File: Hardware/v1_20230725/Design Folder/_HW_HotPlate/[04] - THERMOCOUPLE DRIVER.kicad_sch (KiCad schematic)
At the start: 10 parts, among them J401 RCPT_2POS_2.54MM_VERT, U401 MAX31855JASA+T

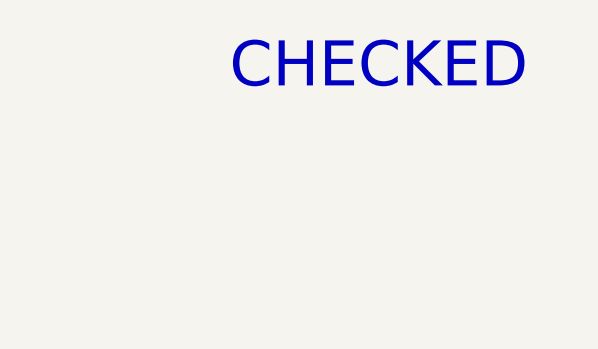
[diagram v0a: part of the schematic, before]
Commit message: Schematic library has been updated
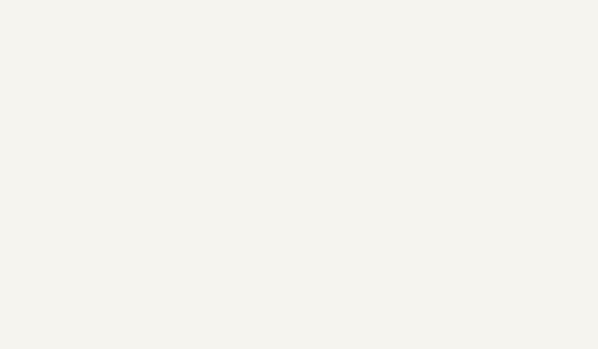
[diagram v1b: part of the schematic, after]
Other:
- note removed: "CHECKED"
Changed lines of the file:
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@@
 (kicad_sch (version 20230121) (generator eeschema)
-  (paper "B")
+  (paper "C")
   (title_block
     (title "Hot Plate")
@@
     (company "Mend0z0")
     (comment 1 "v1")
+    (comment 2 "RELEASED")
     (comment 3 "Siavash Taher Parvar")
     (comment 8 "N/A")
@@
     (effects (font (size 1.27 1.27)) (justify left bottom))
   )
-  (text "CHECKED" (at 378.46 38.1 0)
-    (effects (font (size 5 5)) (justify left bottom))
-  )
   (text "DESIGN NOTE:\n\nIt is strongly recommended \nto add a 10nF ceramic surface-mount\ndifferential capacitor, placed across\nthe T+ and T- pins, in order to \nfilter noise on the thermocouple lines.\n"

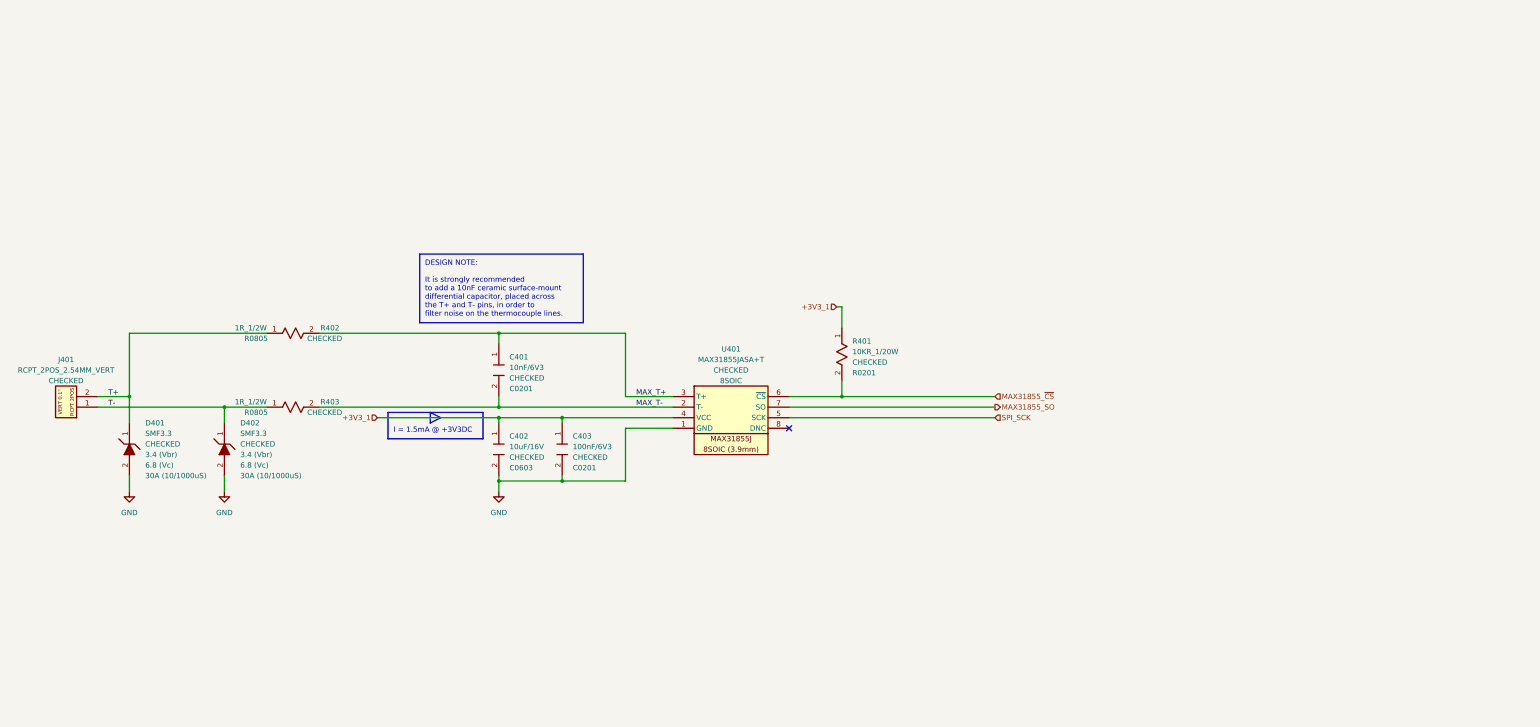
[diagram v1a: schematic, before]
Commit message: components have been updated
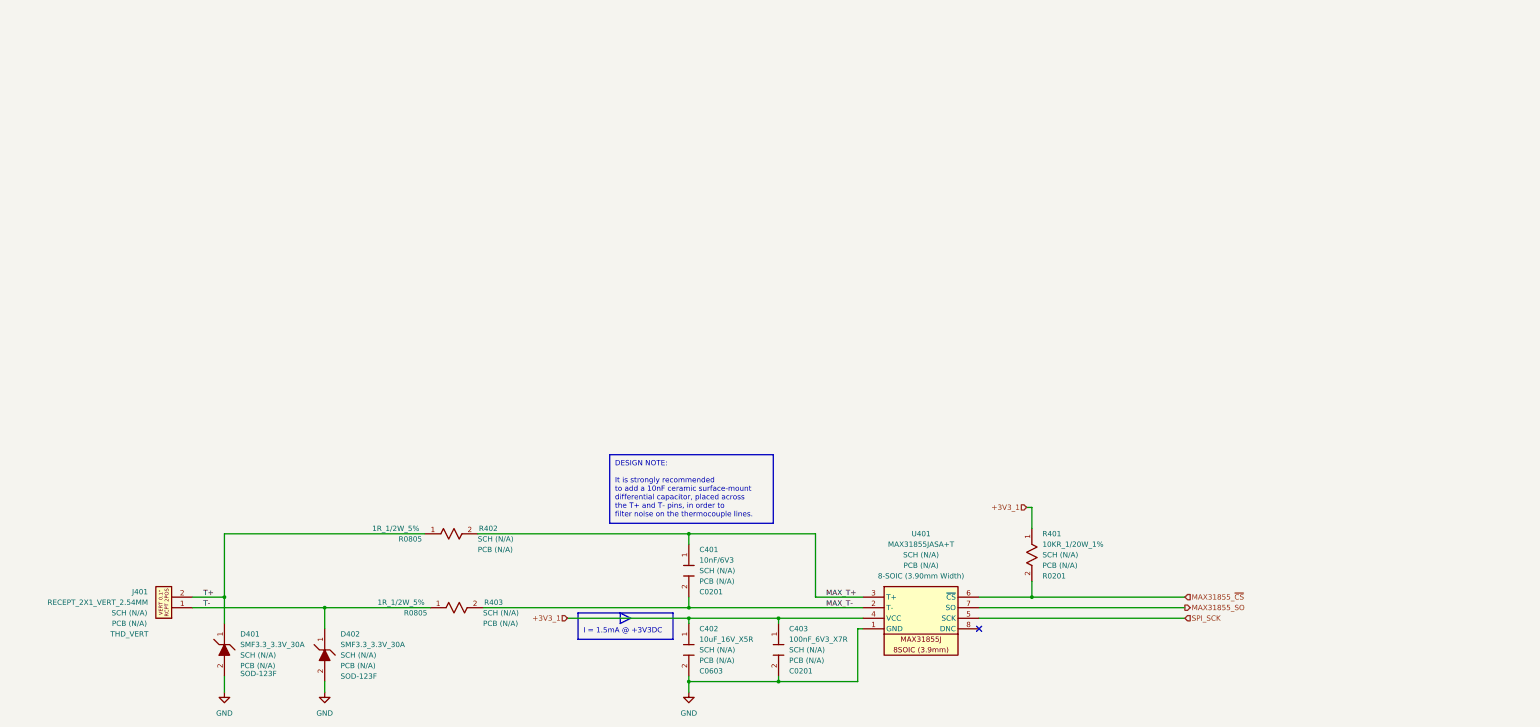
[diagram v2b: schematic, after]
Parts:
- C401: symbol _SCHLIB_HotPlate:CAP_10nF/6V3-C0201 -> _SCHLIB_HotPlate:CAP_10nF_6V3_X7R_C0201; Manufacturer (none) -> Walsin Technology Corporation; PCB CHECk (none) -> PCB (N/A); Part Number 0201B103K6R3CT -> (none); Part Number (Manufacturer) (none) -> 0201B103K6R3CT; Part Number (Vendor) (none) -> 1292-1120-2-ND; SCH CHECK CHECKED -> SCH (N/A); Vendor (none) -> Digikey
- C402: value 10uF/16V -> 10uF_16V_X5R; symbol _SCHLIB_HotPlate:CAP_10uF/16V-C0603 -> _SCHLIB_HotPlate:CAP_10uF_16V_X5R_C0603; Manufacturer (none) -> Murata Electronics; PCB CHECk (none) -> PCB (N/A); Part Number GRT188R61C106KE13J -> (none); Part Number (Manufacturer) (none) -> GRT188R61C106KE13J; Part Number (Vendor) (none) -> 490-GRT188R61C106KE13JTR-ND; SCH CHECK CHECKED -> SCH (N/A); Vendor (none) -> Digikey
- C403: value 100nF/6V3 -> 100nF_6V3_X7R; symbol _SCHLIB_HotPlate:CAP_100nF/6V3_C0201 -> _SCHLIB_HotPlate:CAP_100nF_6V3_X7R_C0201; Manufacturer (none) -> YAGEO; PCB CHECk (none) -> PCB (N/A); Part Number CC0201KRX7R5BB104 -> (none); Part Number (Manufacturer) (none) -> CC0201KRX7R5BB104; Part Number (Vendor) (none) -> 13-CC0201KRX7R5BB104TR-ND; SCH CHECK CHECKED -> SCH (N/A); Vendor (none) -> Digikey
- D401, D402: value SMF3.3 -> SMF3.3_3.3V_30A; symbol _SCHLIB_HotPlate:TVS_SMF3.3_SOD_123F -> _SCHLIB_HotPlate:DIODE_TVS_SMF3.3_3.3V_3.4V_30A(10/1000us)_SOD_123F; Ipp 30A (10/1000uS) -> (none); Manufacturer (none) -> Littelfuse Inc.; PCB CHECk (none) -> PCB (N/A); Package (none) -> SOD-123F; Part Number SMF3.3 -> (none); Part Number (Manufacturer) (none) -> SMF3.3; Part Number (Vendor) (none) -> F7701TR-ND; SCH CHECK CHECKED -> SCH (N/A); Vbr 3.4 (Vbr) -> (none); Vc 6.8 (Vc) -> (none); Vendor (none) -> Digikey
- J401: value RCPT_2POS_2.54MM_VERT -> RECEPT_2X1_VERT_2.54MM; symbol _SCHLIB_HotPlate:CONN_RCPT_2POS_2.54MM_VERT -> _SCHLIB_HotPlate:CONN_RECEPT_2POS_VERT_2.54MM; Manufacturer (none) -> Adam Tech; PCB CHECk (none) -> PCB (N/A); Package (none) -> THD_VERT; Part Number RS1-02-G -> (none); Part Number (Manufacturer) (none) -> RS1-02-G; Part Number (Vendor) (none) -> 2057-RS1-02-G-ND; SCH CHECK CHECKED -> SCH (N/A); Vendor (none) -> Digikey
- R401: value 10KR_1/20W -> 10KR_1/20W_1%; symbol _SCHLIB_HotPlate:RES_10KR_1/20W-R0201 -> _SCHLIB_HotPlate:RES_10KR_1/20W_1%_R0201; Manufacturer (none) -> Stackpole Electronics Inc; PCB CHECk (none) -> PCB (N/A); Part Number RMCF0201FT10K0 -> (none); Part Number (Manufacturer) (none) -> RMCF0201FT10K0; Part Number (Vendor) (none) -> RMCF0201FT10K0TR-ND; SCH CHECK CHECKED -> SCH (N/A); Vendor (none) -> Digikey
- R402, R403: value 1R_1/2W -> 1R_1/2W_5%; symbol _SCHLIB_HotPlate:RES_1R_1/2W_R0805 -> _SCHLIB_HotPlate:RES_1R_1/2W_5%_R0805; Manufacturer (none) -> KOA Speer Electronics, Inc.; PCB CHECk (none) -> PCB (N/A); Part Number SG73P2ATTD1R0J -> (none); Part Number (Manufacturer) (none) -> SG73P2ATTD1R0J; Part Number (Vendor) (none) -> 2019-SG73P2ATTD1R0JTR-ND; SCH CHECK CHECKED -> SCH (N/A); Vendor (none) -> Digikey
- U401: symbol _SCHLIB_HotPlate:IC_MAX31855JASA+T -> _SCHLIB_HotPlate:IC_CONV_MAX31855JASA+T_THERMOCOUPLE_3.3V_8-SOIC; Manufacturer (none) -> Analog Devices Inc./Maxim Integrated; PCB CHECk (none) -> PCB (N/A); Package 8SOIC -> 8-SOIC (3.90mm Width); Part Number MAX31855JASA+T -> (none); Part Number (Manufacturer) (none) -> MAX31855JASA+T; Part Number (Vendor) (none) -> MAX31855JASA+TTR-ND; SCH CHECK CHECKED -> SCH (N/A); Vendor (none) -> Digikey
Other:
- moved on the sheet: C401, C402, C403, D401, D402, J401, R401, R402, R403, U401

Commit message: Updating hardware format structure
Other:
- note added: "DESIGN NOTE:"
- note added: "It is strongly recommended to add a 10nF ceramic surface-mount differential capacitor, placed across the T+ and T- pins, in order to filter noise on the thermocouple lines."
- note removed: "DESIGN NOTE: It is strongly recommended to add a 10nF ceramic surface-mount differential capacitor, placed across the T+ and T- pins, in order to filter noise on the thermocouple lines."
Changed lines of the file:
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@@
+    (stroke (width 0) (type default))
+  )
+  (polyline (pts (xy 189.23 125.73) (xy 189.23 144.78))
     (stroke (width 0) (type default))
   )
@@
   )
   (wire (pts (xy 236.22 176.53) (xy 236.22 177.8))
+    (stroke (width 0) (type default))
+  )
+  (polyline (pts (xy 187.96 124.46) (xy 187.96 146.05))
+    (stroke (width 0) (type default))
+  )
+  (polyline (pts (xy 234.95 124.46) (xy 234.95 146.05))
     (stroke (width 0) (type default))
   )
@@
     (stroke (width 0) (type default))
   )
+  (polyline (pts (xy 233.68 125.73) (xy 233.68 144.78))
+    (stroke (width 0) (type default))
+  )
+  (polyline (pts (xy 189.23 125.73) (xy 233.68 125.73))
+    (stroke (width 0) (type default))
+  )
   (wire (pts (xy 214.63 191.77) (xy 236.22 191.77))
     (stroke (width 0) (type default))
@@
   )
   (wire (pts (xy 284.48 176.53) (xy 334.01 176.53))
+    (stroke (width 0) (type default))
+  )
+  (polyline (pts (xy 187.96 146.05) (xy 234.95 146.05))
     (stroke (width 0) (type default))
   )
@@
     (stroke (width 0) (type default))
   )
+  (polyline (pts (xy 187.96 124.46) (xy 234.95 124.46))
+    (stroke (width 0) (type default))
+  )
   (wire (pts (xy 236.22 191.77) (xy 255.27 191.77))
     (stroke (width 0) (type default))
@@
     (stroke (width 0) (type default))
   )
+  (polyline (pts (xy 233.68 144.78) (xy 189.23 144.78))
+    (stroke (width 0) (type default))
+  )
   (wire (pts (xy 236.22 190.5) (xy 236.22 191.77))
     (stroke (width 0) (type default))
   )
-  (rectangle (start 195.58 137.16) (end 234.95 153.67)
+  (rectangle (start 190.5 127) (end 232.41 143.51)
     (stroke (width 0) (type default))
     (fill (type none))
+  )
+  (text "DESIGN NOTE:" (at 191.77 130.81 0)
+    (effects (font (size 1.8 1.8) bold) (justify left bottom))
   )
   (text "I = 1.5mA @ +3V3DC" (at 189.23 180.34 0)
     (effects (font (size 1.27 1.27)) (justify left bottom))
   )
-  (text "DESIGN NOTE:\n\nIt is strongly recommended \nto add a 10nF ceramic surface-mount\ndifferential capacitor, placed across\nthe T+ and T- pins, in order to \nfilter noise on the thermocouple lines.\n"
-    (at 196.85 152.4 0)
+  (text "\nIt is strongly recommended \nto add a 10nF ceramic surface-mount\ndifferential capacitor, placed across\nthe T+ and T- pins, in order to \nfilter noise on the thermocouple lines.\n"
+    (at 191.77 142.24 0)
     (effects (font (size 1.27 1.27)) (justify left bottom))
   )
